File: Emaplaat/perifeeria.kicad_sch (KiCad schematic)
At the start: 22 parts, among them J3 Conn_01x05_Socket, Q1 2N7002K

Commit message: ketamine addict
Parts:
- removed C270: 100n, symbol Device:C
- removed R213, R214: R, symbol Device:R
- removed S3, S6: Keyswitch, symbol ScottoKeebs:Placeholder_Keyswitch
- added C271: 100n, symbol Device:C
- added D10, D11, D12, D13, D14, D5: PESD1ETH10L-QYL, PESD1ETH10LQYL, symbol PESD1ETH10L-QYL:PESD1ETH10L-QYL
- added R203, R204: 10K, symbol Device:R
- added S4, S5: Keyswitch, symbol ScottoKeebs:Placeholder_Keyswitch
- R2, R216: value R -> 10K
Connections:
- net 3V3: now also R203.1, R204.1
- net AGND: now also S1., S2., C271.2, D10.2 (K2), D11.2 (K2), D12.2 (K2), D13.2 (K2), D14.2 (K2), D5.2 (K2), S4., S5.; no longer S1.2, S2.2
- net BOOT: now also D13.1 (K1)
- net EN: now also D14.1 (K1)
- net Key1: now also R216.2, D5.1 (K1), S4.; no longer S2.1
- net Key2: now also C271.1, D10.1 (K1), R203.2, S5.; no longer C5.1, R2.2, S1.1
- net Key3: now also R2.2, S1., D11.1 (K1); no longer R216.2
- net Key4: now also C5.1, S2., D12.1 (K1), R204.2

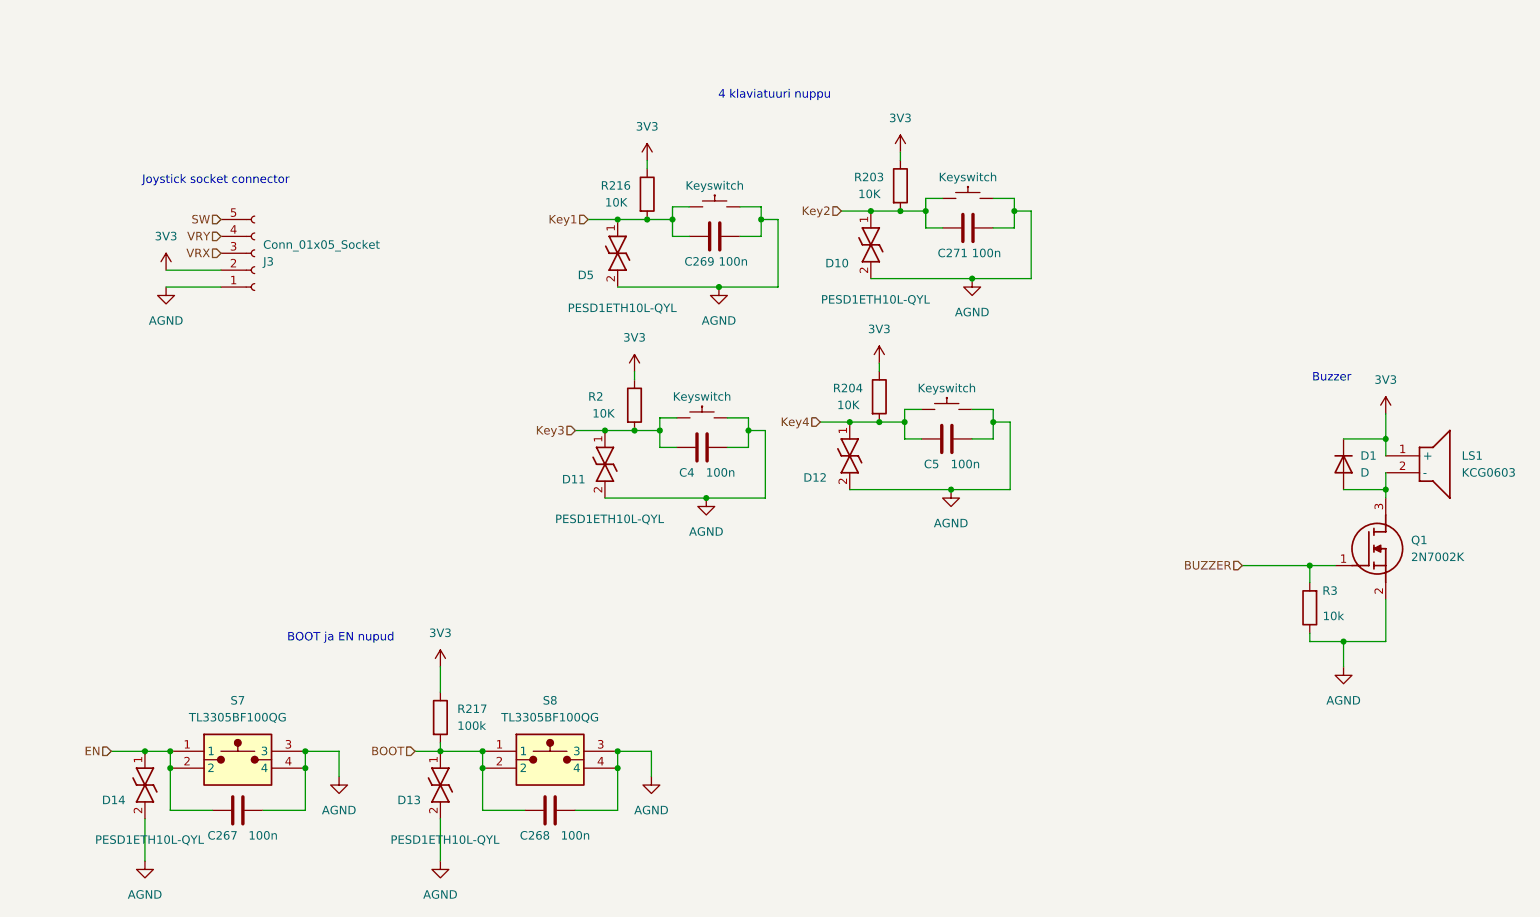
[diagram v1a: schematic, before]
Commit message: 3V3 voolud kontrollitud
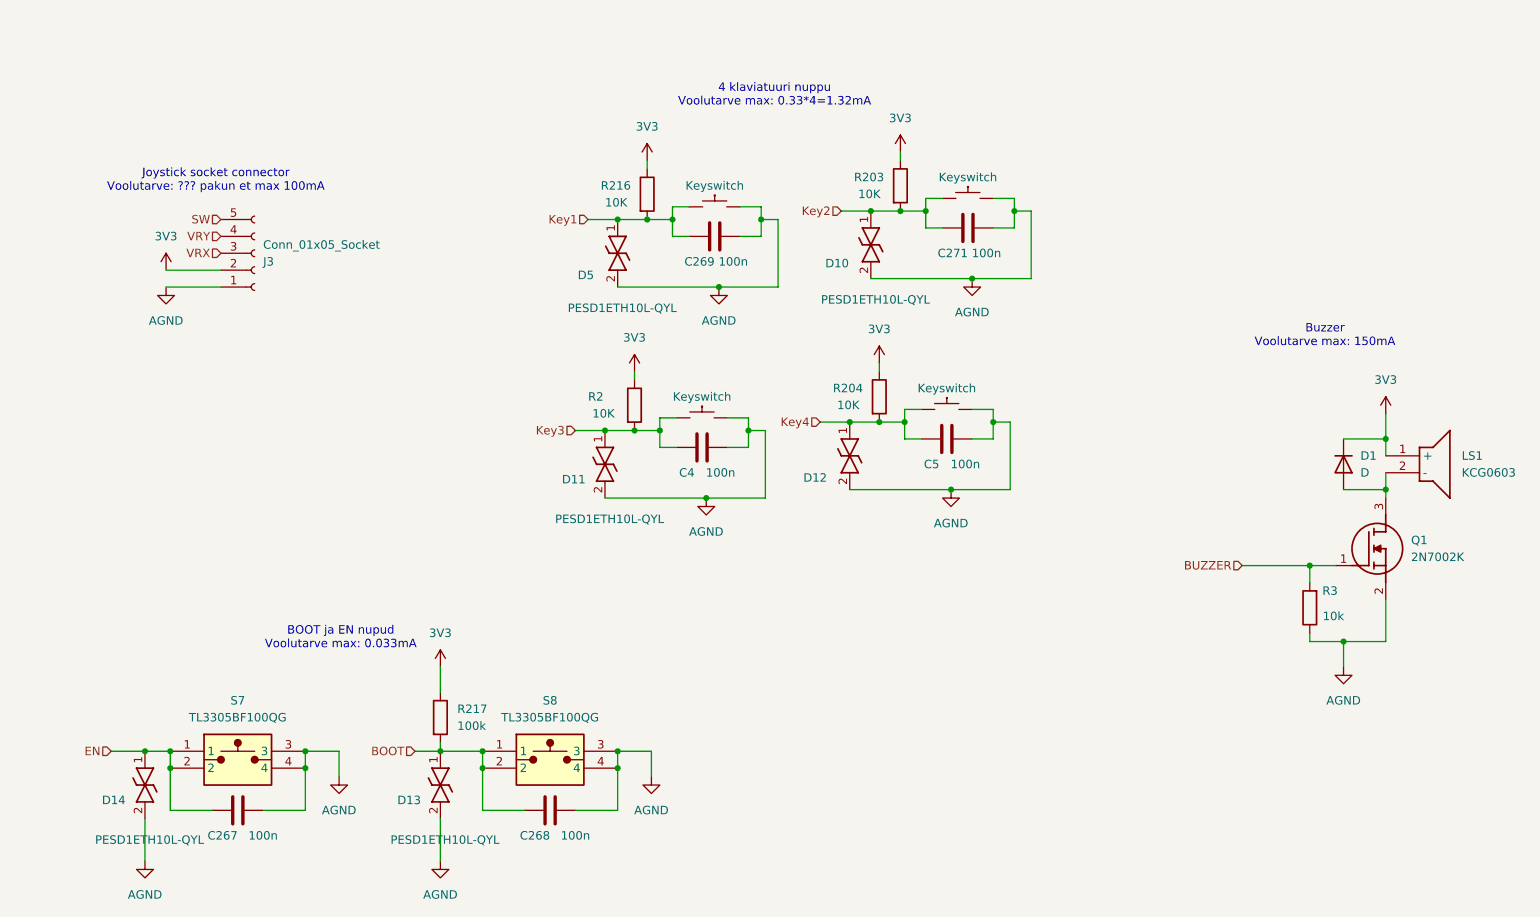
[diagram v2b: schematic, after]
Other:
- note added: "4 klaviatuuri nuppu Voolutarve max: 0.33*4=1.32mA"
- note added: "BOOT ja EN nupud Voolutarve max: 0.033mA"
- note added: "Buzzer Voolutarve max: 150mA"
- note added: "Joystick socket connector Voolutarve: ??? pakun et max 100mA"
- note removed: "4 klaviatuuri nuppu"
- note removed: "BOOT ja EN nupud"
- note removed: "Buzzer"
- note removed: "Joystick socket connector"
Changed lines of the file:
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@@
 	(generator_version "9.0")
 	(paper "A4")
-	(text "Buzzer"
+	(text "Buzzer\nVoolutarve max: 150mA"
 		(exclude_from_sim no)
-		(at 231.902 93.726 0)
+		(at 230.886 87.376 0)
 		(effects
 			(font
@@
 		)
 	)
-	(text "4 klaviatuuri nuppu"
+	(text "4 klaviatuuri nuppu\nVoolutarve max: 0.33*4=1.32mA"
 		(exclude_from_sim no)
 		(at 148.082 51.181 0)
@@
 		)
 	)
-	(text "Joystick socket connector"
+	(text "Joystick socket connector\nVoolutarve: ??? pakun et max 100mA"
 		(exclude_from_sim no)
 		(at 64.008 64.008 0)
@@
 		)
 	)
-	(text "BOOT ja EN nupud"
+	(text "BOOT ja EN nupud\nVoolutarve max: 0.033mA"
 		(exclude_from_sim no)
 		(at 82.804 132.842 0)

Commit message: okei fix
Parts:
- removed D10, D11, D12, D13, D14, D5: PESD1ETH10L-QYL, PESD1ETH10LQYL, symbol PESD1ETH10L-QYL:PESD1ETH10L-QYL
- added D10, D11, D12, D13, D14, D5: CPDH3V3UP-HF, SODFL1608X77N, symbol CPDH3V3UP-HF:CPDH3V3UP-HF
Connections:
- net AGND: now also D10. (A), D11. (A), D12. (A), D13. (A), D14. (A), D5. (A)
- net BOOT: now also D14. (A)
- net EN: now also D13. (A)
- net Key1: now also D5. (A)
- net Key2: now also D10. (A)
- net Key3: now also D11. (A)
- net Key4: now also D12. (A)

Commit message: jajald
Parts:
- removed D1: D, symbol Device:D
- added D14: D, SOD-123FL:SOD-123FL, symbol Device:D
- C49: renamed from C271; footprint (none) -> Capacitor_SMD:C_0603_1608Metric_Pad1.08x0.95mm_HandSolder
- C50: renamed from C269; footprint (none) -> Capacitor_SMD:C_0603_1608Metric_Pad1.08x0.95mm_HandSolder
- C51: renamed from C5; footprint (none) -> Capacitor_SMD:C_0603_1608Metric_Pad1.08x0.95mm_HandSolder
- C52: renamed from C4; footprint (none) -> Capacitor_SMD:C_0603_1608Metric_Pad1.08x0.95mm_HandSolder
- C53: renamed from C267; footprint (none) -> Capacitor_SMD:C_0603_1608Metric_Pad1.08x0.95mm_HandSolder
- C54: renamed from C268; footprint (none) -> Capacitor_SMD:C_0603_1608Metric_Pad1.08x0.95mm_HandSolder
- J3: footprint (none) -> Connector_PinSocket_2.54mm:PinSocket_1x05_P2.54mm_Horizontal
- R75: renamed from R203; footprint (none) -> Resistor_SMD:R_0603_1608Metric_Pad0.98x0.95mm_HandSolder
- R76: renamed from R216; footprint (none) -> Resistor_SMD:R_0603_1608Metric_Pad0.98x0.95mm_HandSolder
- R77: renamed from R204; footprint (none) -> Resistor_SMD:R_0603_1608Metric_Pad0.98x0.95mm_HandSolder
- R78: renamed from R2; footprint (none) -> Resistor_SMD:R_0603_1608Metric_Pad0.98x0.95mm_HandSolder
- R80: renamed from R217; footprint (none) -> Resistor_SMD:R_0603_1608Metric_Pad0.98x0.95mm_HandSolder
- S1: renamed from S5; footprint (none) -> Button_Switch_Keyboard:SW_Cherry_MX_1.00u_PCB
- S2: renamed from S4; footprint (none) -> Button_Switch_Keyboard:SW_Cherry_MX_1.00u_PCB
- S3: renamed from S2; footprint (none) -> Button_Switch_Keyboard:SW_Cherry_MX_1.00u_PCB
- S4: renamed from S1; footprint (none) -> Button_Switch_Keyboard:SW_Cherry_MX_1.00u_PCB
- renumbered D5 to D11, D11 to D13, D13 to D15, D14 to D16, R3 to R79, S7 to S5, S8 to S6
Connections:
- net 3V3: now also D14.2 (A)
- net at LS1.2 (-), Q1.3 (D): now also D14.1 (K)

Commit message: skeem korras
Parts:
- D10, D11, D12, D13, D15, D16: footprint SODFL1608X77N -> Diode_SMD:D_SOD-523
- LS1: footprint KCG0603 -> KCG0603:KCG0603
- Q1: footprint SOT95P240X120-3N -> SOT95P240X120-3N:SOT95P240X120-3N
- S5, S6: footprint TL3305BF160QG -> TL3305BF160QG:TL3305BF160QG

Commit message: trükkplaat algus
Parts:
- R79: footprint (none) -> Resistor_SMD:R_0603_1608Metric_Pad0.98x0.95mm_HandSolder
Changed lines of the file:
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@@
 			)
 		)
-		(property "Footprint" ""
+		(property "Footprint" "Resistor_SMD:R_0603_1608Metric_Pad0.98x0.95mm_HandSolder"
 			(at 230.378 128.27 90)
 			(effects

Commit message: bonkers
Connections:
- net AGND: now also D10.2 (A), D11.2 (A), D12.2 (A), D13.2 (A), D15.2 (A), D16.2 (A); no longer D10. (A), D11. (A), D12. (A), D13. (A), D15. (A), D16. (A)
- net BOOT: now also D16.1 (K); no longer D16. (A)
- net EN: now also D15.1 (K); no longer D15. (A)
- net Key1: now also D11.1 (K); no longer D11. (A)
- net Key2: now also D10.1 (K); no longer D10. (A)
- net Key3: now also D13.1 (K); no longer D13. (A)
- net Key4: now also D12.1 (K); no longer D12. (A)

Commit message: :TTT: WWKWKWWKWWKWWKWKWWKWW !"]¤3!E_#1%FV{'14¤#(%2
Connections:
- net 3V3: no longer R75.1, R76.1, R77.1, R78.1
- net AGND: no longer C49.2, C50.2, C51.2, C52.2, C54.2, D10.2 (A), D11.2 (A), D12.2 (A), D13.2 (A), D15.2 (A), D16.2 (A), J3.1 (Pin_1), Q1.2 (S), R79.1, S1., S2., S3., S4., S6.3, S6.4
- net Key1: now also R76.1, S2.1; no longer R76.2, S2.
- net Key2: now also R75.1, S1.1; no longer R75.2, S1.
- net Key3: now also R78.1, S4.1; no longer R78.2, S4.
- net Key4: now also R77.1, S3.1; no longer R77.2, S3.
- new net GND: C49.2, C50.2, C51.2, C52.2, C54.2, D10.2 (A), D11.2 (A), D12.2 (A), D13.2 (A), D15.2 (A), D16.2 (A), J3.1 (Pin_1), Q1.2 (S), R75.2, R76.2, R77.2, R78.2, R79.1, S1.2, S2.2, S3.2, S4.2, S6.3, S6.4
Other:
- moved on the sheet: C49, C50, C51, C52, D10, D11, D12, D13, R75, R76, R77, R78
